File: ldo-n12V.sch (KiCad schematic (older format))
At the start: 8 parts

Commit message: change LDO sch capacitors & finish component selection
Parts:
- removed C?: 22u, symbol Device:C
- added C?: 4.7u, Capacitor_SMD:C_0805_2012Metric_Pad1.15x1.40mm_HandSolder, symbol Device:C
- C?: footprint (none) -> Capacitor_SMD:C_0805_2012Metric_Pad1.15x1.40mm_HandSolder; Description (none) -> CAP CER 10UF 16V X5R 0805; Manufacturer (none) -> Taiyo Yuden; Manufacturer Part Number (none) -> EMK212ABJ106KD-T; Supplier (none) -> Digi-Key; Supplier Part Number (none) -> 587-2980-1-ND
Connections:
- net -12Vreg: now also C?.2
- net GND: now also C?.1
- net at R?.1, U?.8 (SET): now also C?.2; no longer C?.2
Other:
- moved on the sheet: C?
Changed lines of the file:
@@
 L Device:C C?
 U 1 1 5CA61EE0
-P 4750 3950
+P 7050 4200
 AR Path="/5C87B3B6/5CA61EE0" Ref="C?"  Part="1"
 AR Path="/5CA59CF7/5CA61EE0" Ref="C?"  Part="1"
 AR Path="/5CA59CFA/5CA61EE0" Ref="C?"  Part="1"
-F 0 "C?" H 4635 3904 50  0000 R CNN
-F 1 "10u" H 4635 3995 50  0000 R CNN
-F 2 "" H 4788 3800 50  0001 C CNN
-F 3 "" H 4750 3950 50  0001 C CNN
-F 4 "" H 2300 -1200 50  0001 C CNN "Description"
-F 5 "" H 2300 -1200 50  0001 C CNN "Manufacturer"
-F 6 "" H 2300 -1200 50  0001 C CNN "Manufacturer Part Number"
-F 7 "" H 2300 -1200 50  0001 C CNN "Supplier"
-F 8 "" H 2300 -1200 50  0001 C CNN "Supplier Part Number"
-	1    4750 3950
-	1    0    0    -1
+F 0 "C?" H 6935 4154 50  0000 R CNN
+F 1 "10u" H 6935 4245 50  0000 R CNN
+F 2 "Capacitor_SMD:C_0805_2012Metric_Pad1.15x1.40mm_HandSolder" H 7088 4050 50  0001 C CNN
+F 3 "https://www.yuden.co.jp/productdata/catalog/mlcc07_e.pdf" H 7050 4200 50  0001 C CNN
+F 4 "CAP CER 10UF 16V X5R 0805" H 4600 -950 50  0001 C CNN "Description"
+F 5 "Taiyo Yuden" H 4600 -950 50  0001 C CNN "Manufacturer"
+F 6 "EMK212ABJ106KD-T" H 4600 -950 50  0001 C CNN "Manufacturer Part Number"
+F 7 "Digi-Key" H 4600 -950 50  0001 C CNN "Supplier"
+F 8 "587-2980-1-ND" H 4600 -950 50  0001 C CNN "Supplier Part Number"
+	1    7050 4200
+	-1   0    0    -1
 $EndComp
 Wire Wire Line
@@
 Wire Wire Line
 	6850 3700 5900 3700
-$Comp
-L Device:C C?
-U 1 1 5CA61F1B
-P 7050 4200
-AR Path="/5C87B3B6/5CA61F1B" Ref="C?"  Part="1"
-AR Path="/5CA59CF7/5CA61F1B" Ref="C?"  Part="1"
-AR Path="/5CA59CFA/5CA61F1B" Ref="C?"  Part="1"
-F 0 "C?" H 6935 4154 50  0000 R CNN
-F 1 "22u" H 6935 4245 50  0000 R CNN
-F 2 "" H 7088 4050 50  0001 C CNN
-F 3 "" H 7050 4200 50  0001 C CNN
-F 4 "" H 4600 -950 50  0001 C CNN "Description"
-F 5 "" H 4600 -950 50  0001 C CNN "Manufacturer"
-F 6 "" H 4600 -950 50  0001 C CNN "Manufacturer Part Number"
-F 7 "" H 4600 -950 50  0001 C CNN "Supplier"
-F 8 "" H 4600 -950 50  0001 C CNN "Supplier Part Number"
-	1    7050 4200
-	-1   0    0    -1
-$EndComp
 Wire Wire Line
 	6850 4700 7050 4700
@@
 Text Notes 5350 5100 0    50   ~ 0
 EN/UV resistor divider sets IC enable threshold
+$Comp
+L Device:C C?
+U 1 1 5D039BC5
+P 4750 3950
+AR Path="/5C87B3B6/5D039BC5" Ref="C?"  Part="1"
+AR Path="/5C903B7C/5D039BC5" Ref="C?"  Part="1"
+AR Path="/5CA59CFA/5D039BC5" Ref="C?"  Part="1"
+F 0 "C?" H 4635 3904 50  0000 R CNN
+F 1 "4.7u" H 4635 3995 50  0000 R CNN
+F 2 "Capacitor_SMD:C_0805_2012Metric_Pad1.15x1.40mm_HandSolder" H 4788 3800 50  0001 C CNN
+F 3 "https://www.yuden.co.jp/productdata/catalog/mlcc01_e.pdf" H 4750 3950 50  0001 C CNN
+F 4 "CAP CER 4.7UF 10V X5R 0805" H 1450 400 50  0001 C CNN "Description"
+F 5 "Taiyo Yuden" H 1450 400 50  0001 C CNN "Manufacturer"
+F 6 "LMK212BJ475KD-T" H 1450 400 50  0001 C CNN "Manufacturer Part Number"
+F 7 "Digi-Key" H 1450 400 50  0001 C CNN "Supplier"
+F 8 "587-1297-1-ND" H 1450 400 50  0001 C CNN "Supplier Part Number"
+	1    4750 3950
+	1    0    0    -1
+$EndComp
 $EndSCHEMATC

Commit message: add components for audo.sch
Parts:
- R?: Description RES SMD 121K OHM 0.1% 1/8W 0805 Thin Film -> RES SMD 121K OHM 0.1% 1/8W 0805 Metal Film
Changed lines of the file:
@@
 F 2 "Resistor_SMD:R_0805_2012Metric_Pad1.15x1.40mm_HandSolder" V 4880 3950 50  0001 C CNN
 F 3 "https://industrial.panasonic.com/cdbs/www-data/pdf/RDM0000/AOA0000C307.pdf" H 4950 3950 50  0001 C CNN
-F 4 "RES SMD 121K OHM 0.1% 1/8W 0805 Thin Film" H 4950 3950 50  0001 C CNN "Description"
+F 4 "RES SMD 121K OHM 0.1% 1/8W 0805 Metal Film" H 4950 3950 50  0001 C CNN "Description"
 F 5 "Panasonic Electronic Components" H 4950 3950 50  0001 C CNN "Manufacturer"
 F 6 "ERA-6AEB1213V" H 4950 3950 50  0001 C CNN "Manufacturer Part Number"

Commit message: switch components supplier to Mouser for price/availability
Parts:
- C?: Supplier Digi-Key -> Mouser; Supplier Part Number 587-1297-1-ND -> 963-LMK212BJ475KD-T
- U?: Supplier Digi-Key -> Mouser; Supplier Part Number LT3094EMSE#PBF-ND -> 584-LT3094EMSE#PBF
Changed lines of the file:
@@
 F 5 "Linear Technology" H 0   0   50  0001 C CNN "Manufacturer"
 F 6 "LT3094EMSE#PBF" H 0   0   50  0001 C CNN "Manufacturer Part Number"
-F 7 "Digi-Key" H 0   0   50  0001 C CNN "Supplier"
-F 8 "LT3094EMSE#PBF-ND" H 0   0   50  0001 C CNN "Supplier Part Number"
+F 7 "Mouser" H 0   0   50  0001 C CNN "Supplier"
+F 8 "584-LT3094EMSE#PBF" H 0   0   50  0001 C CNN "Supplier Part Number"
 	1    5900 4450
 	1    0    0    -1
@@
 F 5 "Taiyo Yuden" H 1450 400 50  0001 C CNN "Manufacturer"
 F 6 "LMK212BJ475KD-T" H 1450 400 50  0001 C CNN "Manufacturer Part Number"
-F 7 "Digi-Key" H 1450 400 50  0001 C CNN "Supplier"
-F 8 "587-1297-1-ND" H 1450 400 50  0001 C CNN "Supplier Part Number"
+F 7 "Mouser" H 1450 400 50  0001 C CNN "Supplier"
+F 8 "963-LMK212BJ475KD-T" H 1450 400 50  0001 C CNN "Supplier Part Number"
 	1    4750 3950
 	1    0    0    -1

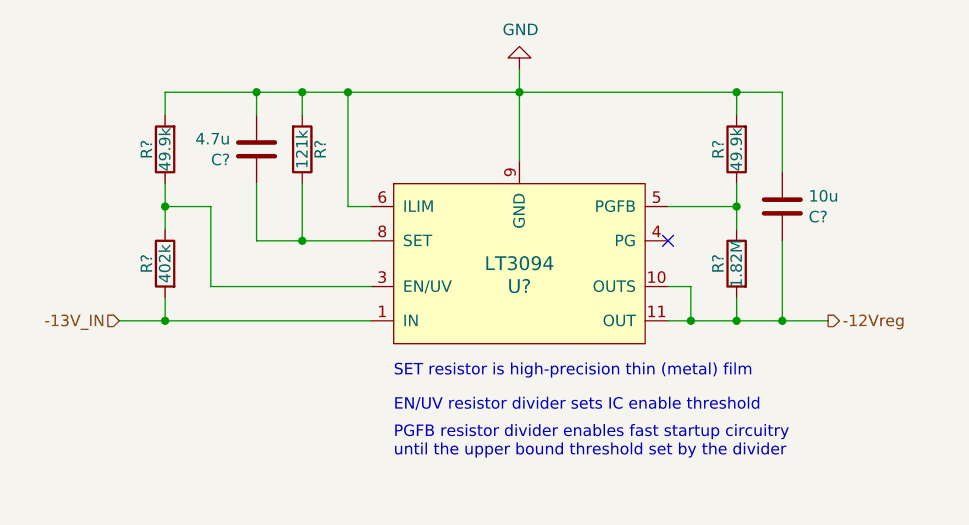
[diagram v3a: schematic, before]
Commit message: update ldo threshold configs & components
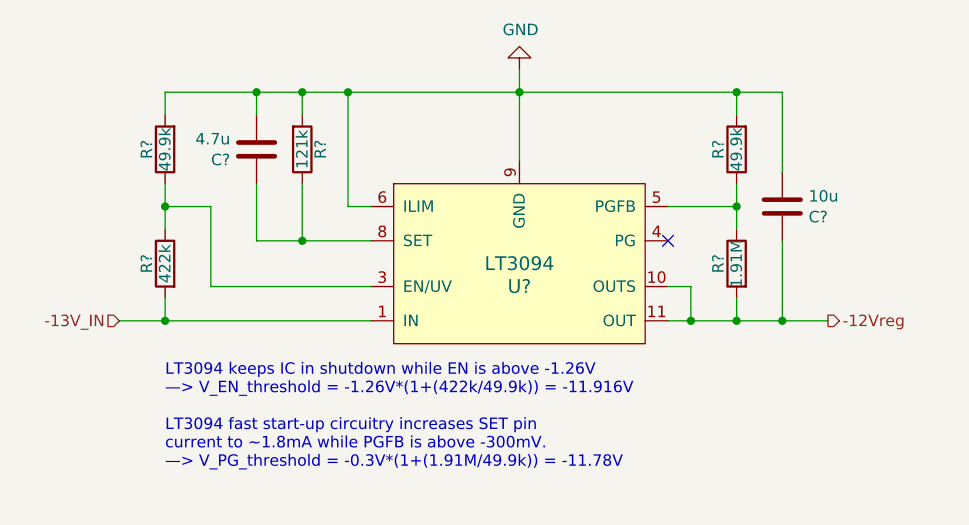
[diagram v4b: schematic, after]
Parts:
- R?: value 1.82M -> 1.91M; Description RES SMD 1.82M OHM 1% 1/8W 0805 -> RES SMD 1.91M OHM 1% 1/8W 0805; Manufacturer Part Number ERJ-6ENF1824V -> ERJ-6ENF1914V; Supplier Part Number P1.82BTCT-ND -> P1.91BTCT-ND
- R?: value 402k -> 422k; Description RES SMD 402K OHM 1% 1/8W 0805 -> RES SMD 422K OHM 1% 1/8W 0805; Manufacturer Part Number ERJ-6ENF4023V -> ERJ-6ENF4223V; Supplier Part Number P402KCCT-ND -> P422KCCT-ND
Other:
- note added: "LT3094 keeps IC in shutdown while EN is above -1.26V\n—> V_EN_threshold = -1.26V*(1+(422k/49.9k)) = -11.916V\n\nLT3094 fast start-up circuitry increases SET pin\ncurrent to ~~1.8mA while PGFB is above -300mV.\n—> V_PG_threshold = -0.3V*(1+(1.91M/49.9k)) = -11.78V"
- note removed: "EN/UV resistor divider sets IC enable threshold"
- note removed: "PGFB resistor divider enables fast startup circuitry\nuntil the upper bound threshold set by the divider"
- note removed: "SET resistor is high-precision thin (metal) film"
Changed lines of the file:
@@
 AR Path="/5CA59CFA/5CA61F03" Ref="R?"  Part="1"
 F 0 "R?" V 6930 4450 50  0000 C CNN
-F 1 "1.82M" V 6850 4450 50  0000 C CNN
+F 1 "1.91M" V 6850 4450 50  0000 C CNN
 F 2 "Resistor_SMD:R_0805_2012Metric_Pad1.15x1.40mm_HandSolder" V 6780 4450 50  0001 C CNN
 F 3 "https://industrial.panasonic.com/cdbs/www-data/pdf/RDA0000/AOA0000C304.pdf" H 6850 4450 50  0001 C CNN
-F 4 "RES SMD 1.82M OHM 1% 1/8W 0805" H 6850 4450 50  0001 C CNN "Description"
+F 4 "RES SMD 1.91M OHM 1% 1/8W 0805" H 6850 4450 50  0001 C CNN "Description"
 F 5 "Panasonic Electronic Components" H 6850 4450 50  0001 C CNN "Manufacturer"
-F 6 "ERJ-6ENF1824V" H 6850 4450 50  0001 C CNN "Manufacturer Part Number"
+F 6 "ERJ-6ENF1914V" H 6850 4450 50  0001 C CNN "Manufacturer Part Number"
 F 7 "Digi-Key" H 6850 4450 50  0001 C CNN "Supplier"
-F 8 "P1.82BTCT-ND" H 6850 4450 50  0001 C CNN "Supplier Part Number"
+F 8 "P1.91BTCT-ND" H 6850 4450 50  0001 C CNN "Supplier Part Number"
 	1    6850 4450
 	-1   0    0    -1
@@
 AR Path="/5CA59CFA/5CAC3636" Ref="R?"  Part="1"
 F 0 "R?" V 4430 4450 50  0000 C CNN
-F 1 "402k" V 4350 4450 50  0000 C CNN
+F 1 "422k" V 4350 4450 50  0000 C CNN
 F 2 "Resistor_SMD:R_0805_2012Metric_Pad1.15x1.40mm_HandSolder" V 4280 4450 50  0001 C CNN
 F 3 "https://industrial.panasonic.com/cdbs/www-data/pdf/RDA0000/AOA0000C304.pdf" H 4350 4450 50  0001 C CNN
-F 4 "RES SMD 402K OHM 1% 1/8W 0805" H 4350 4450 50  0001 C CNN "Description"
+F 4 "RES SMD 422K OHM 1% 1/8W 0805" H 4350 4450 50  0001 C CNN "Description"
 F 5 "Panasonic Electronic Components" H 4350 4450 50  0001 C CNN "Manufacturer"
-F 6 "ERJ-6ENF4023V" H 4350 4450 50  0001 C CNN "Manufacturer Part Number"
+F 6 "ERJ-6ENF4223V" H 4350 4450 50  0001 C CNN "Manufacturer Part Number"
 F 7 "Digi-Key" H 4350 4450 50  0001 C CNN "Supplier"
-F 8 "P402KCCT-ND" H 4350 4450 50  0001 C CNN "Supplier Part Number"
+F 8 "P422KCCT-ND" H 4350 4450 50  0001 C CNN "Supplier Part Number"
 	1    4350 4450
 	-1   0    0    -1
@@
 	1    0    0    1
 $EndComp
-Text Notes 5350 4950 0    50   ~ 0
-SET resistor is high-precision thin (metal) film
-Text Notes 5350 5300 0    50   ~ 0
-PGFB resistor divider enables fast startup circuitry\nuntil the upper bound threshold set by the divider
-Text Notes 5350 5100 0    50   ~ 0
-EN/UV resistor divider sets IC enable threshold
+Text Notes 4350 5350 0    50   ~ 0
+LT3094 keeps IC in shutdown while EN is above -1.26V\n—> V_EN_threshold = -1.26V*(1+(422k/49.9k)) = -11.916V\n\nLT3094 fast start-up circuitry increases SET pin\ncurrent to ~~1.8mA while PGFB is above -300mV.\n—> V_PG_threshold = -0.3V*(1+(1.91M/49.9k)) = -11.78V
 $Comp
 L Device:C C?

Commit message: fix audio pot label & other label sizing
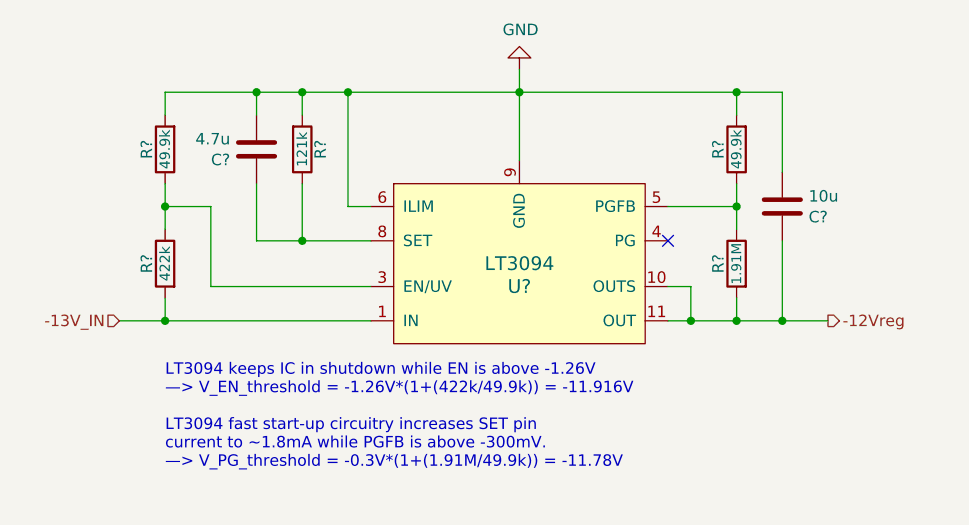
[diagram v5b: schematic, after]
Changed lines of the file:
@@
 AR Path="/5CA59CFA/5CA61F03" Ref="R?"  Part="1"
 F 0 "R?" V 6930 4450 50  0000 C CNN
-F 1 "1.91M" V 6850 4450 50  0000 C CNN
+F 1 "1.91M" V 6850 4450 43  0000 C CNN
 F 2 "Resistor_SMD:R_0805_2012Metric_Pad1.15x1.40mm_HandSolder" V 6780 4450 50  0001 C CNN
 F 3 "https://industrial.panasonic.com/cdbs/www-data/pdf/RDA0000/AOA0000C304.pdf" H 6850 4450 50  0001 C CNN
@@
 AR Path="/5CA59CFA/5CAC3636" Ref="R?"  Part="1"
 F 0 "R?" V 4430 4450 50  0000 C CNN
-F 1 "422k" V 4350 4450 50  0000 C CNN
+F 1 "422k" V 4350 4450 45  0000 C CNN
 F 2 "Resistor_SMD:R_0805_2012Metric_Pad1.15x1.40mm_HandSolder" V 4280 4450 50  0001 C CNN
 F 3 "https://industrial.panasonic.com/cdbs/www-data/pdf/RDA0000/AOA0000C304.pdf" H 4350 4450 50  0001 C CNN
@@
 AR Path="/5CA59CFA/5CAEF591" Ref="R?"  Part="1"
 F 0 "R?" V 4430 3950 50  0000 C CNN
-F 1 "49.9k" V 4350 3950 50  0000 C CNN
+F 1 "49.9k" V 4350 3950 45  0000 C CNN
 F 2 "Resistor_SMD:R_0805_2012Metric_Pad1.15x1.40mm_HandSolder" V 4280 3950 50  0001 C CNN
 F 3 "https://industrial.panasonic.com/cdbs/www-data/pdf/RDA0000/AOA0000C304.pdf" H 4350 3950 50  0001 C CNN
@@
 AR Path="/5CA59CFA/5CAEFC49" Ref="R?"  Part="1"
 F 0 "R?" V 6930 3950 50  0000 C CNN
-F 1 "49.9k" V 6850 3950 50  0000 C CNN
+F 1 "49.9k" V 6850 3950 45  0000 C CNN
 F 2 "Resistor_SMD:R_0805_2012Metric_Pad1.15x1.40mm_HandSolder" V 6780 3950 50  0001 C CNN
 F 3 "https://industrial.panasonic.com/cdbs/www-data/pdf/RDA0000/AOA0000C304.pdf" H 6850 3950 50  0001 C CNN
@@
 AR Path="/5CA59CFA/5CAF0F36" Ref="R?"  Part="1"
 F 0 "R?" V 5030 3950 50  0000 C CNN
-F 1 "121k" V 4950 3950 50  0000 C CNN
+F 1 "121k" V 4950 3950 45  0000 C CNN
 F 2 "Resistor_SMD:R_0805_2012Metric_Pad1.15x1.40mm_HandSolder" V 4880 3950 50  0001 C CNN
 F 3 "https://industrial.panasonic.com/cdbs/www-data/pdf/RDM0000/AOA0000C307.pdf" H 4950 3950 50  0001 C CNN

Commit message: add circuit notes
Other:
- note added: "LT3094 keeps IC in shutdown while EN is above -1.26V\n—> V_EN_threshold = -1.26V*(1+(422k/49.9k)) = -11.916V\n\nLT3094 fast start-up circuitry increases SET pin\ncurrent to ~~1.8mA while PGFB is above -300mV.\n—> V_PG_threshold = -0.3V*(1+(1.91M/49.9k)) = -11.78V\n\nV_o = -I_SET * R_SET = -100uA * 121k = -12.1V"
- note removed: "LT3094 keeps IC in shutdown while EN is above -1.26V\n—> V_EN_threshold = -1.26V*(1+(422k/49.9k)) = -11.916V\n\nLT3094 fast start-up circuitry increases SET pin\ncurrent to ~~1.8mA while PGFB is above -300mV.\n—> V_PG_threshold = -0.3V*(1+(1.91M/49.9k)) = -11.78V"
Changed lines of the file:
@@
 	1    0    0    1
 $EndComp
-Text Notes 4350 5350 0    50   ~ 0
-LT3094 keeps IC in shutdown while EN is above -1.26V\n—> V_EN_threshold = -1.26V*(1+(422k/49.9k)) = -11.916V\n\nLT3094 fast start-up circuitry increases SET pin\ncurrent to ~~1.8mA while PGFB is above -300mV.\n—> V_PG_threshold = -0.3V*(1+(1.91M/49.9k)) = -11.78V
+Text Notes 4350 5500 0    50   ~ 0
+LT3094 keeps IC in shutdown while EN is above -1.26V\n—> V_EN_threshold = -1.26V*(1+(422k/49.9k)) = -11.916V\n\nLT3094 fast start-up circuitry increases SET pin\ncurrent to ~~1.8mA while PGFB is above -300mV.\n—> V_PG_threshold = -0.3V*(1+(1.91M/49.9k)) = -11.78V\n\nV_o = -I_SET * R_SET = -100uA * 121k = -12.1V
 $Comp
 L Device:C C?
